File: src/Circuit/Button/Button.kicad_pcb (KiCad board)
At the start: 2 copper layers, 17 x 15 mm, 5 parts, among them K1 CONN_3, SW1 SW_PUSH

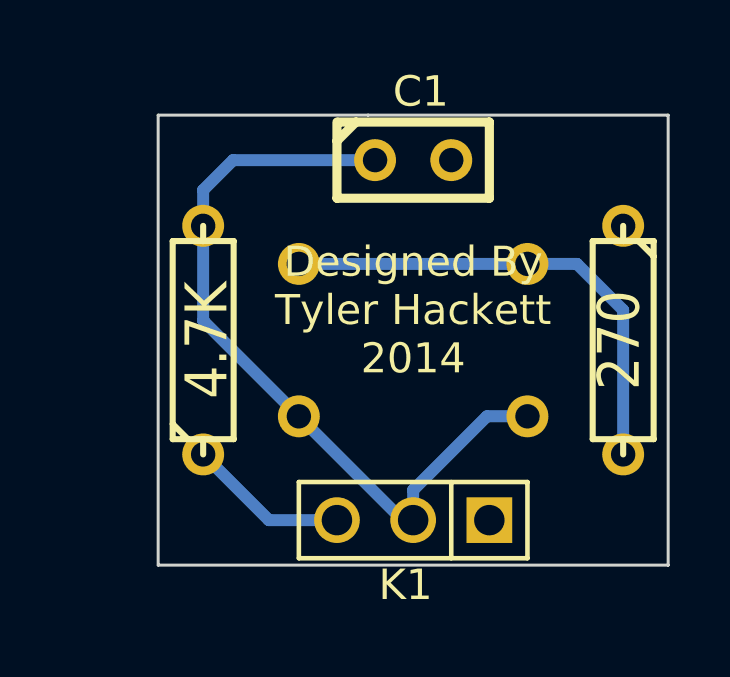
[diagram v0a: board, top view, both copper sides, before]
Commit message: Widened hole on cube circuit, smaller button PCB
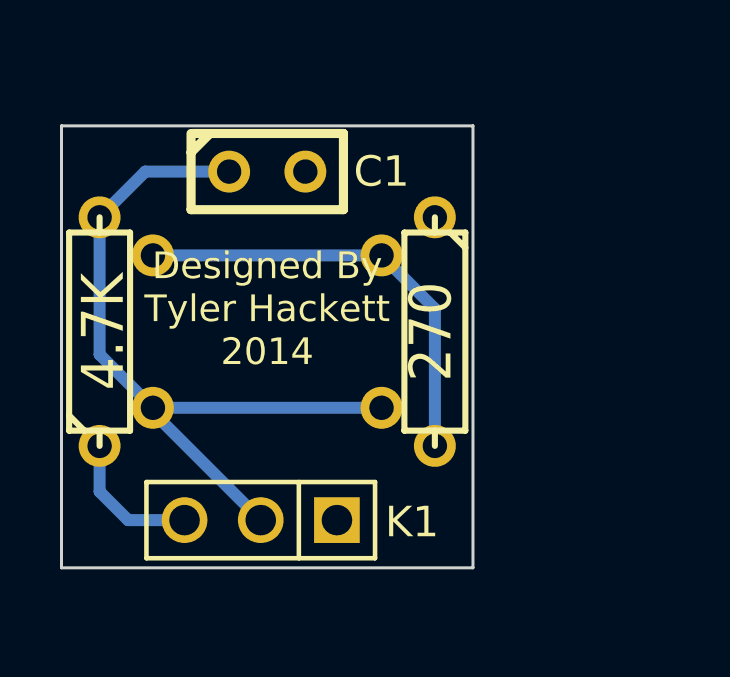
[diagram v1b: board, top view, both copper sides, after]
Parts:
- moved R2 6.28 mm to (204.7, 140.7)
- moved K1 5.08 mm to (198.9, 147.0)
- moved C1 4.88 mm to (199.1, 135.4)
- moved SW1 4.87 mm to (199.1, 140.7)
- moved R1 3.46 mm to (193.5, 140.7)
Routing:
- net N-000001: track 16.3 -> 14.7 mm
- net N-000002: track 26.1 -> 24.9 mm
- net VCC: track 5.37 -> 4.75 mm
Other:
- board size 17 x 15 mm -> 13.7 x 14.7 mm
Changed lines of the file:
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@@
     (links 9)
     (no_connects 0)
-    (area 195.449999 131.8504 212.550001 149.9972)
+    (area 192.176399 132.2324 206.095601 149.9972)
     (thickness 1.6)
-    (drawings 6)
-    (tracks 16)
+    (drawings 5)
+    (tracks 13)
     (zones 0)
     (modules 5)
@@
     (pad_to_mask_clearance 0)
     (aux_axis_origin 0 0)
-    (visible_elements FFFFFFBF)
+    (visible_elements 7FFFFFFF)
     (pcbplotparams
       (layerselection 3178497)
@@
   )
   (module SW_PUSH_SMALL (layer B.Cu)
-    (at 204 141)
+    (at 199.136 140.716)
     (fp_text reference SW1 (at 0 0.762) (layer B.SilkS)
       (effects (font (size 1.016 1.016) (thickness 0.2032)) (justify mirror))
@@
   )
   (module R3 (layer F.Cu)
-    (at 211 141 270)
+    (at 204.724 140.716 270)
     (descr "Resitance 3 pas")
     (tags R)
@@
   )
   (module R3 (layer F.Cu)
-    (at 197 141 90)
+    (at 193.548 140.716 90)
     (descr "Resitance 3 pas")
     (tags R)
@@
   )
   (module PIN_ARRAY_3X1 (layer F.Cu)
-    (at 204 147 180)
+    (at 198.92 147 180)
     (descr "Connecteur 3 pins")
     (tags "CONN DEV")
-    (fp_text reference K1 (at 0.254 -2.159 180) (layer F.SilkS)
+    (fp_text reference K1 (at -5.042 -0.066 180) (layer F.SilkS)
       (effects (font (size 1.016 1.016) (thickness 0.1524)))
     )
@@
   )
   (module C1 (layer F.Cu)
-    (at 204 135)
+    (at 199.136 135.382)
     (descr "Condensateur e = 1 pas")
     (tags C)
-    (fp_text reference C1 (at 0.254 -2.286) (layer F.SilkS)
+    (fp_text reference C1 (at 3.81 0) (layer F.SilkS)
       (effects (font (size 1.016 1.016) (thickness 0.2032)))
     )
@@
     )
   )
-  (gr_text "Designed By\nTyler Hackett\n2014" (at 204 140) (layer F.SilkS)
-    (effects (font (size 1 1) (thickness 0.25)))
-  )
-  (gr_line (start 212.5 133.5) (end 202.5 133.5) (angle 90) (layer Edge.Cuts) (width 0.1))
-  (gr_line (start 212.5 148.5) (end 212.5 133.5) (angle 90) (layer Edge.Cuts) (width 0.1))
-  (gr_line (start 195.5 148.5) (end 212.5 148.5) (angle 90) (layer Edge.Cuts) (width 0.1))
-  (gr_line (start 195.5 133.5) (end 195.5 148.5) (angle 90) (layer Edge.Cuts) (width 0.1))
-  (gr_line (start 202.5 133.5) (end 195.5 133.5) (angle 90) (layer Edge.Cuts) (width 0.1))
-  (segment (start 200.19 138.46) (end 207.81 138.46) (width 0.4) (layer B.Cu) (net 2))
-  (segment (start 207.81 138.46) (end 209.46 138.46) (width 0.4) (layer B.Cu) (net 2))
-  (segment (start 211 140) (end 211 144.81) (width 0.4) (layer B.Cu) (net 2))
-  (segment (start 209.46 138.46) (end 211 140) (width 0.4) (layer B.Cu) (net 2))
-  (segment (start 207.81 143.54) (end 206.46 143.54) (width 0.4) (layer B.Cu) (net 3))
-  (segment (start 204 146) (end 204 147) (width 0.4) (layer B.Cu) (net 3))
-  (segment (start 206.46 143.54) (end 204 146) (width 0.4) (layer B.Cu) (net 3))
-  (segment (start 197 137.19) (end 197 140.35) (width 0.4) (layer B.Cu) (net 3))
-  (segment (start 197 140.35) (end 200.19 143.54) (width 0.4) (layer B.Cu) (net 3))
-  (segment (start 197 137.19) (end 197 136) (width 0.4) (layer B.Cu) (net 3))
-  (segment (start 198 135) (end 202.73 135) (width 0.4) (layer B.Cu) (net 3))
-  (segment (start 197 136) (end 198 135) (width 0.4) (layer B.Cu) (net 3))
-  (segment (start 204 147) (end 203.65 147) (width 0.4) (layer B.Cu) (net 3))
-  (segment (start 203.65 147) (end 200.19 143.54) (width 0.4) (layer B.Cu) (net 3))
-  (segment (start 201.46 147) (end 199.19 147) (width 0.4) (layer B.Cu) (net 4))
-  (segment (start 199.19 147) (end 197 144.81) (width 0.4) (layer B.Cu) (net 4))
+  (gr_line (start 205.994 133.858) (end 192.278 133.858) (angle 90) (layer Edge.Cuts) (width 0.1))
+  (gr_line (start 205.994 148.59) (end 205.994 133.858) (angle 90) (layer Edge.Cuts) (width 0.1))
+  (gr_line (start 192.278 148.59) (end 205.994 148.59) (angle 90) (layer Edge.Cuts) (width 0.1))
+  (gr_line (start 192.278 133.858) (end 192.278 148.59) (angle 90) (layer Edge.Cuts) (width 0.1))
+  (gr_text "Designed By\nTyler Hackett\n2014" (at 199.136 139.954) (layer F.SilkS)
+    (effects (font (size 0.889 0.889) (thickness 0.22225)))
+  )
+  (segment (start 204.724 144.526) (end 204.724 139.954) (width 0.4) (layer B.Cu) (net 2))
+  (segment (start 204.724 139.954) (end 202.946 138.176) (width 0.4) (layer B.Cu) (net 2))
+  (segment (start 195.326 138.176) (end 202.946 138.176) (width 0.4) (layer B.Cu) (net 2))
+  (segment (start 195.326 143.256) (end 195.326 143.406) (width 0.4) (layer B.Cu) (net 3))
+  (segment (start 195.326 143.406) (end 198.92 147) (width 0.4) (layer B.Cu) (net 3))
+  (segment (start 195.326 143.256) (end 202.946 143.256) (width 0.4) (layer B.Cu) (net 3))
+  (segment (start 193.548 136.906) (end 193.548 141.478) (width 0.4) (layer B.Cu) (net 3))
+  (segment (start 193.548 141.478) (end 195.326 143.256) (width 0.4) (layer B.Cu) (net 3))
+  (segment (start 197.866 135.382) (end 195.072 135.382) (width 0.4) (layer B.Cu) (net 3))
+  (segment (start 195.072 135.382) (end 193.548 136.906) (width 0.4) (layer B.Cu) (net 3))
+  (segment (start 196.38 147) (end 194.498 147) (width 0.4) (layer B.Cu) (net 4))
+  (segment (start 193.548 146.05) (end 193.548 144.526) (width 0.4) (layer B.Cu) (net 4))
+  (segment (start 194.498 147) (end 193.548 146.05) (width 0.4) (layer B.Cu) (net 4))
   (zone (net 1) (net_name GND) (layer F.Cu) (hatch edge 0.508)
     (connect_pads (clearance 0.508))
@@
     (polygon
       (pts
-        (xy 212.5 148.5) (xy 195.5 148.5) (xy 195.5 133.5) (xy 212.5 133.5)
+        (xy 205.994 148.59) (xy 192.278 148.59) (xy 192.278 133.858) (xy 205.994 133.858)
       )
     )

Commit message: Adjusted the pin header on button PCB
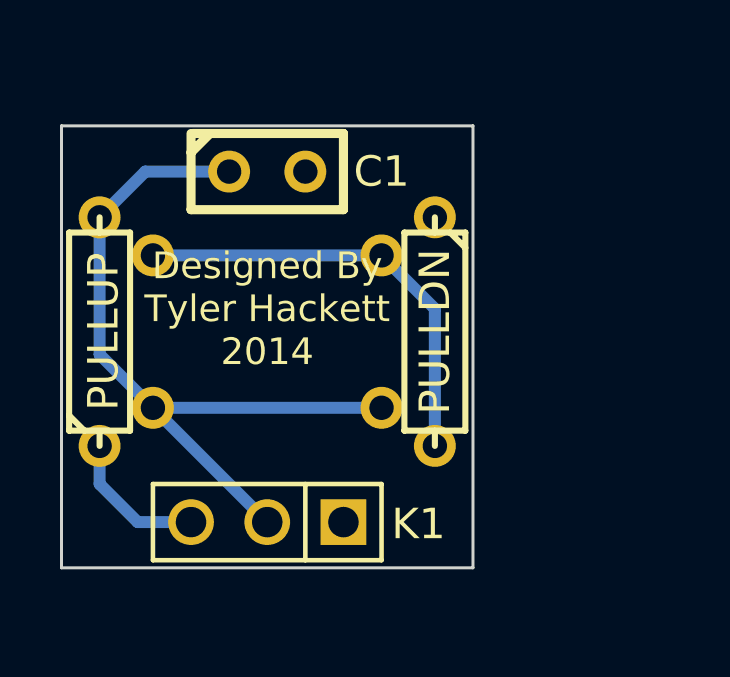
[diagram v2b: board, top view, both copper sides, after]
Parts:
- R1: value 4.7K -> PULLUP
- R2: value 270 -> PULLDN
- moved K1 0.23 mm to (199.1, 147.1)
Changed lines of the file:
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@@
     (links 9)
     (no_connects 0)
-    (area 192.176399 132.2324 206.095601 149.9972)
+    (area 192.176399 132.2324 206.095601 150.0632)
     (thickness 1.6)
     (drawings 5)
-    (tracks 13)
+    (tracks 12)
     (zones 0)
     (modules 5)
@@
     (visible_elements 7FFFFFFF)
     (pcbplotparams
-      (layerselection 3178497)
+      (layerselection 284196865)
       (usegerberextensions true)
       (excludeedgelayer true)
@@
       (plotinvisibletext false)
       (padsonsilk false)
-      (subtractmaskfromsilk false)
+      (subtractmaskfromsilk true)
       (outputformat 1)
       (mirror false)
-      (drillshape 1)
+      (drillshape 0)
       (scaleselection 1)
-      (outputdirectory ""))
+      (outputdirectory S:/Users/TyDesktop/Documents/GitHub/3D-LED-Companion-Cube/src/Circuit/Button/Gerber/))
   )
   (net 0 "")
@@
       (effects (font (size 1.397 1.27) (thickness 0.2032)))
     )
-    (fp_text value 270 (at 0 0.127 270) (layer F.SilkS)
-      (effects (font (size 1.397 1.27) (thickness 0.2032)))
+    (fp_text value PULLDN (at 0 0 270) (layer F.SilkS)
+      (effects (font (size 1.016 1.016) (thickness 0.2032)))
     )
     (fp_line (start -3.81 0) (end -3.302 0) (layer F.SilkS) (width 0.2032))
@@
       (effects (font (size 1.397 1.27) (thickness 0.2032)))
     )
-    (fp_text value 4.7K (at 0 0.127 90) (layer F.SilkS)
-      (effects (font (size 1.397 1.27) (thickness 0.2032)))
+    (fp_text value PULLUP (at 0 0.127 90) (layer F.SilkS)
+      (effects (font (size 1.016 1.016) (thickness 0.2032)))
     )
     (fp_line (start -3.81 0) (end -3.302 0) (layer F.SilkS) (width 0.2032))
@@
   )
   (module PIN_ARRAY_3X1 (layer F.Cu)
-    (at 198.92 147 180)
+    (at 199.136 147.066 180)
     (descr "Connecteur 3 pins")
     (tags "CONN DEV")
@@
   (segment (start 204.724 139.954) (end 202.946 138.176) (width 0.4) (layer B.Cu) (net 2))
   (segment (start 195.326 138.176) (end 202.946 138.176) (width 0.4) (layer B.Cu) (net 2))
-  (segment (start 195.326 143.256) (end 195.326 143.406) (width 0.4) (layer B.Cu) (net 3))
-  (segment (start 195.326 143.406) (end 198.92 147) (width 0.4) (layer B.Cu) (net 3))
+  (segment (start 199.136 147.066) (end 195.326 143.256) (width 0.4) (layer B.Cu) (net 3))
   (segment (start 195.326 143.256) (end 202.946 143.256) (width 0.4) (layer B.Cu) (net 3))
   (segment (start 193.548 136.906) (end 193.548 141.478) (width 0.4) (layer B.Cu) (net 3))
@@
   (segment (start 197.866 135.382) (end 195.072 135.382) (width 0.4) (layer B.Cu) (net 3))
   (segment (start 195.072 135.382) (end 193.548 136.906) (width 0.4) (layer B.Cu) (net 3))
-  (segment (start 196.38 147) (end 194.498 147) (width 0.4) (layer B.Cu) (net 4))
-  (segment (start 193.548 146.05) (end 193.548 144.526) (width 0.4) (layer B.Cu) (net 4))
-  (segment (start 194.498 147) (end 193.548 146.05) (width 0.4) (layer B.Cu) (net 4))
+  (segment (start 193.548 144.526) (end 193.548 145.796) (width 0.4) (layer B.Cu) (net 4))
+  (segment (start 194.818 147.066) (end 196.596 147.066) (width 0.4) (layer B.Cu) (net 4))
+  (segment (start 193.548 145.796) (end 194.818 147.066) (width 0.4) (layer B.Cu) (net 4))
   (zone (net 1) (net_name GND) (layer F.Cu) (hatch edge 0.508)
     (connect_pads (clearance 0.508))
